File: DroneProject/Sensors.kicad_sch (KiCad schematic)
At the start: 21 parts, among them U61 LSM6DSOTR, U62 TMAG5273C1QDBVR, U63 INA181A1IDBVR, U64 M24C02-WMN6TP

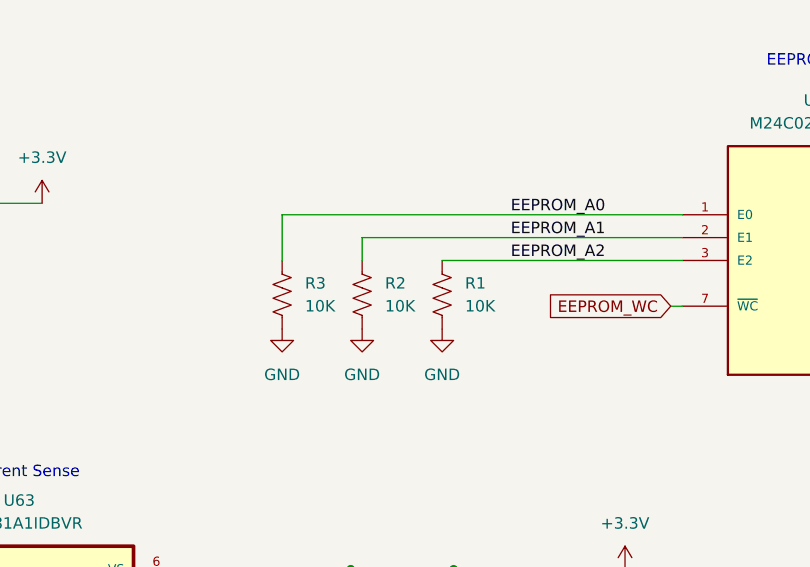
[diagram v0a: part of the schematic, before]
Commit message: Added test points
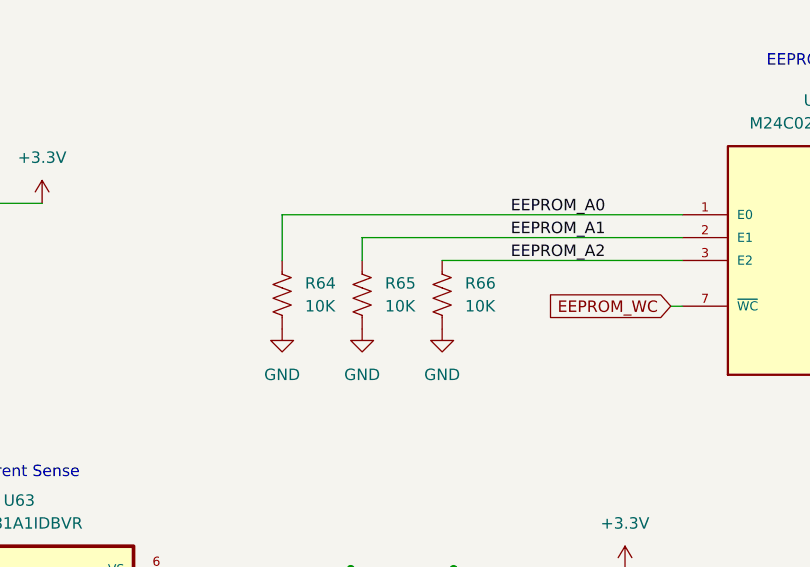
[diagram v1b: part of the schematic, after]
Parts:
- renumbered R3 to R64, R2 to R65, R1 to R66
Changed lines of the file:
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@@
 		(dnp no)
 		(fields_autoplaced yes)
-		(property "Reference" "R1"
+		(property "Reference" "R66"
 			(at 171.45 91.4399 0)
 			(effects
@@
 			(project "DroneProject"
 				(path "/feb4ca7b-5376-4689-a73b-f56020a5aa30/7cfdeeab-6878-42e6-abbb-2c878b968332"
-					(reference "R1")
+					(reference "R66")
 					(unit 1)
 				)
@@
 		(dnp no)
 		(fields_autoplaced yes)
-		(property "Reference" "R3"
+		(property "Reference" "R64"
 			(at 153.67 91.4399 0)
 			(effects
@@
 			(project "DroneProject"
 				(path "/feb4ca7b-5376-4689-a73b-f56020a5aa30/7cfdeeab-6878-42e6-abbb-2c878b968332"
-					(reference "R3")
+					(reference "R64")
 					(unit 1)
 				)
@@
 		(dnp no)
 		(fields_autoplaced yes)
-		(property "Reference" "R2"
+		(property "Reference" "R65"
 			(at 162.56 91.4399 0)
 			(effects
@@
 			(project "DroneProject"
 				(path "/feb4ca7b-5376-4689-a73b-f56020a5aa30/7cfdeeab-6878-42e6-abbb-2c878b968332"
-					(reference "R2")
-					(unit 1)
-				)
+					(reference "R65")
+					(unit 1)
+				)

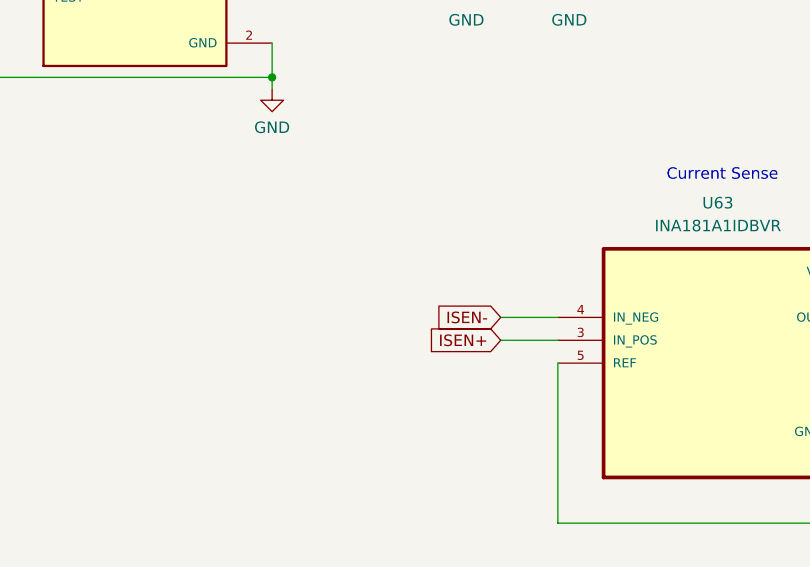
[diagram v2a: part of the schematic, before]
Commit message: Finished initial PCB layout.  However decided to go ahead and add the motor drivers for the first prototype anyways.  Re-did the reverse-polarity detection to use an NMOS instead of a PMOS.  Added sheets for each motor, still need to decide on parts.
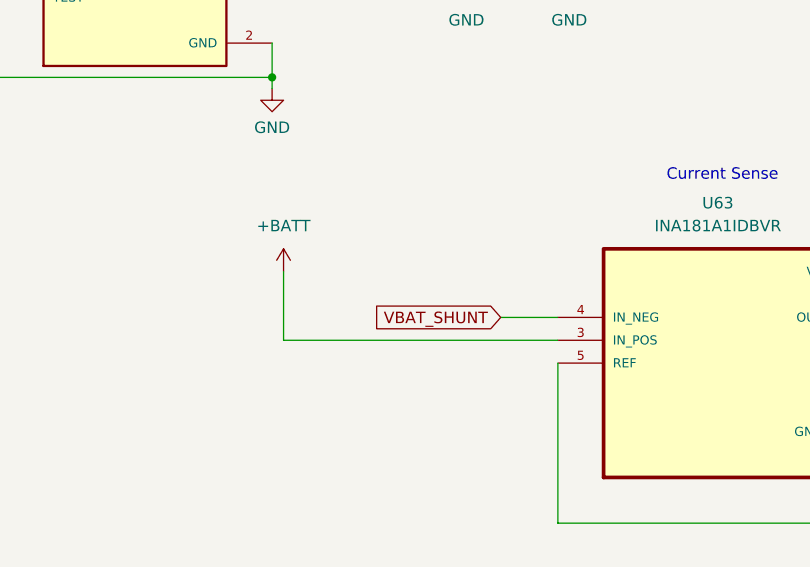
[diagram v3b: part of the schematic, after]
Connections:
- net ISEN+ renamed +BATT
- net ISEN- renamed VBAT_SHUNT
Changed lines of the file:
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@@
+	(wire
+		(pts
+			(xy 72.39 101.6) (xy 72.39 102.87)
+		)
+		(stroke
+			(width 0)
+			(type default)
+		)
+	)
+	(wire
+		(pts
+			(xy 93.98 82.55) (xy 105.41 82.55)
+		)
+		(stroke
+			(width 0)
+			(type default)
+		)
+	)
+	(wire
+		(pts
+			(xy 160.02 88.9) (xy 160.02 86.36)
+		)
+		(stroke
+			(width 0)
+			(type default)
+		)
+	)
+	(wire
+		(pts
+			(xy 92.71 36.83) (xy 95.25 36.83)
+		)
+		(stroke
+			(width 0)
+			(type default)
+		)
+	)
+	(wire
+		(pts
+			(xy 226.06 83.82) (xy 228.6 83.82)
+		)
+		(stroke
+			(width 0)
+			(type default)
+		)
+	)
+	(wire
+		(pts
+			(xy 151.13 88.9) (xy 151.13 83.82)
+		)
+		(stroke
+			(width 0)
+			(type default)
+		)
+	)
 	(wire
 		(pts
@@
 	(wire
 		(pts
-			(xy 72.39 101.6) (xy 72.39 102.87)
-		)
-		(stroke
-			(width 0)
-			(type default)
-		)
-	)
-	(wire
-		(pts
-			(xy 93.98 82.55) (xy 105.41 82.55)
-		)
-		(stroke
-			(width 0)
-			(type default)
-		)
-	)
-	(wire
-		(pts
-			(xy 160.02 88.9) (xy 160.02 86.36)
-		)
-		(stroke
-			(width 0)
-			(type default)
-		)
-	)
-	(wire
-		(pts
-			(xy 92.71 36.83) (xy 95.25 36.83)
-		)
-		(stroke
-			(width 0)
-			(type default)
-		)
-	)
-	(wire
-		(pts
-			(xy 226.06 83.82) (xy 228.6 83.82)
-		)
-		(stroke
-			(width 0)
-			(type default)
-		)
-	)
-	(wire
-		(pts
-			(xy 151.13 88.9) (xy 151.13 83.82)
-		)
-		(stroke
-			(width 0)
-			(type default)
-		)
-	)
-	(wire
-		(pts
 			(xy 55.88 46.99) (xy 67.31 46.99)
 		)
@@
 	(wire
 		(pts
+			(xy 73.66 123.19) (xy 73.66 130.81)
+		)
+		(stroke
+			(width 0)
+			(type default)
+		)
+	)
+	(wire
+		(pts
 			(xy 151.13 83.82) (xy 195.58 83.82)
 		)
@@
 	(wire
 		(pts
+			(xy 104.14 130.81) (xy 73.66 130.81)
+		)
+		(stroke
+			(width 0)
+			(type default)
+		)
+	)
+	(wire
+		(pts
 			(xy 226.06 78.74) (xy 247.65 78.74)
 		)
@@
 		(pts
 			(xy 83.82 39.37) (xy 95.25 39.37)
-		)
-		(stroke
-			(width 0)
-			(type default)
-		)
-	)
-	(wire
-		(pts
-			(xy 97.79 130.81) (xy 104.14 130.81)
 		)
 		(stroke
@@
 		)
 	)
-	(global_label "ISEN-"
+	(global_label "VBAT_SHUNT"
 		(shape input)
 		(at 97.79 128.27 180)
@@
 		)
 		(property "Intersheetrefs" "${INTERSHEET_REFS}"
-			(at 88.9386 128.27 0)
+			(at 83.2538 128.27 0)
 			(effects
 				(font
@@
 		)
 	)
-	(global_label "ISEN+"
+	(global_label "I2C1_SCL"
 		(shape input)
-		(at 97.79 130.81 180)
+		(at 74.93 87.63 0)
 		(fields_autoplaced yes)
 		(effects
@@
 				(size 1.27 1.27)
 			)
-			(justify right)
-		)
-		(property "Intersheetrefs" "${INTERSHEET_REFS}"
-			(at 88.9386 130.81 0)
-			(effects
-				(font
-					(size 1.27 1.27)
-				)
-				(justify right)
-			)
-		)
-	)
-	(global_label "I2C1_SCL"
-		(shape input)
-		(at 74.93 87.63 0)
-		(fields_autoplaced yes)
-		(effects
-			(font
-				(size 1.27 1.27)
-			)
 			(justify left)
 		)
@@
 					(unit 1)
 				)
+			)
+		)
+	)
+	(symbol
+		(lib_id "power:+BATT")
+		(at 73.66 123.19 0)
+		(unit 1)
+		(exclude_from_sim no)
+		(in_bom yes)
+		(on_board yes)
+		(dnp no)
+		(fields_autoplaced yes)
+		(property "Reference" "#PWR07"
+			(at 73.66 127 0)
+			(effects
+				(font
+					(size 1.27 1.27)
+				)
+				(hide yes)
+			)
+		)
+		(property "Value" "+BATT"
+			(at 73.66 118.11 0)
+			(effects
+				(font
+					(size 1.27 1.27)
+				)
+			)
+		)
+		(property "Footprint" ""
+			(at 73.66 123.19 0)
+			(effects
+				(font
+					(size 1.27 1.27)
+				)
+				(hide yes)
+			)
+		)
+		(property "Datasheet" ""
+			(at 73.66 123.19 0)
+			(effects
+				(font
+					(size 1.27 1.27)
+				)
+				(hide yes)
+			)
+		)
+		(property "Description" "Power symbol creates a global label with name \"+BATT\""
+			(at 73.66 123.19 0)
+			(effects
+				(font
+					(size 1.27 1.27)
+				)
+				(hide yes)
+			)
+		)
+		(pin "1"
+		)
+		(instances
+			(project ""
+				(path "/feb4ca7b-5376-4689-a73b-f56020a5aa30/7cfdeeab-6878-42e6-abbb-2c878b968332"
+					(reference "#PWR07")
+					(unit 1)
+				)

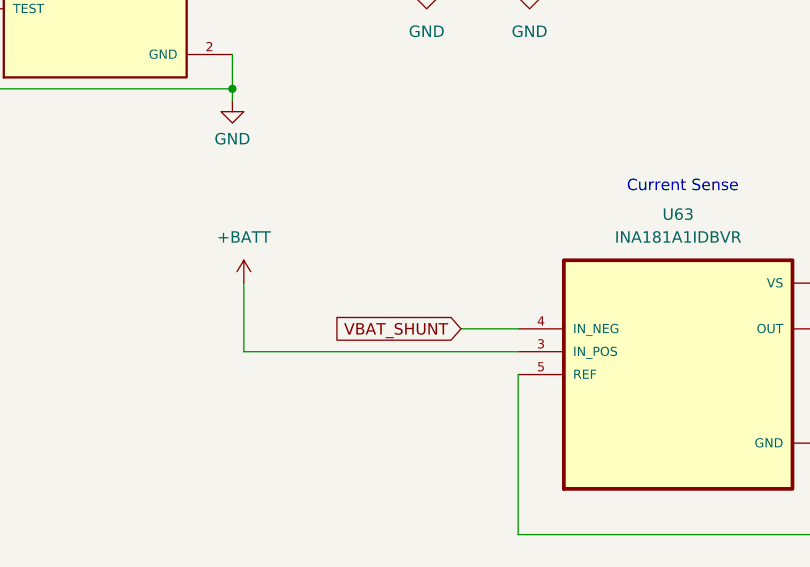
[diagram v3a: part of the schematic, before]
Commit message: Re-did layout for new power system
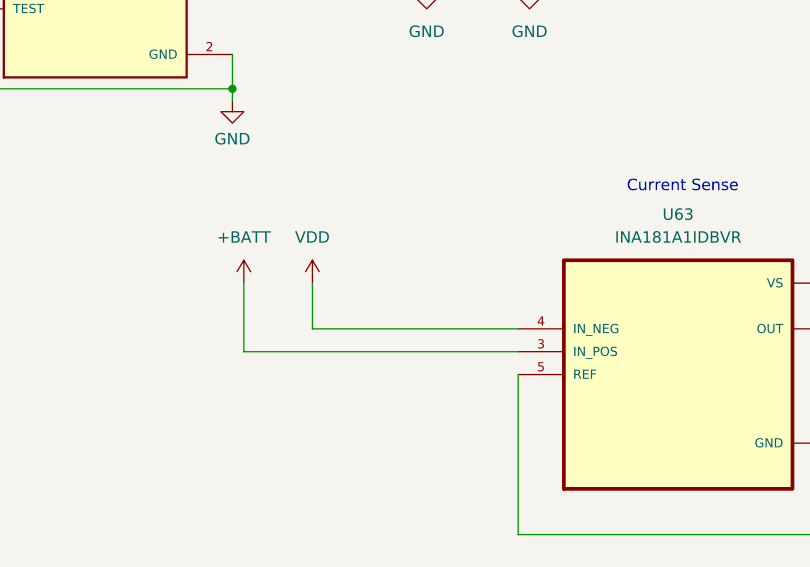
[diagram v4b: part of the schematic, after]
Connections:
- net VBAT_SHUNT renamed VDD
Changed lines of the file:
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@@
-	(wire
-		(pts
-			(xy 97.79 128.27) (xy 104.14 128.27)
-		)
-		(stroke
-			(width 0)
-			(type default)
-		)
-	)
 	(wire
 		(pts
@@
 	(wire
 		(pts
+			(xy 81.28 123.19) (xy 81.28 128.27)
+		)
+		(stroke
+			(width 0)
+			(type default)
+		)
+	)
+	(wire
+		(pts
 			(xy 24.13 46.99) (xy 24.13 43.18)
+		)
+		(stroke
+			(width 0)
+			(type default)
+		)
+	)
+	(wire
+		(pts
+			(xy 81.28 128.27) (xy 104.14 128.27)
 		)
 		(stroke
@@
 				)
 				(justify left)
-			)
-		)
-	)
-	(global_label "VBAT_SHUNT"
-		(shape input)
-		(at 97.79 128.27 180)
-		(fields_autoplaced yes)
-		(effects
-			(font
-				(size 1.27 1.27)
-			)
-			(justify right)
-		)
-		(property "Intersheetrefs" "${INTERSHEET_REFS}"
-			(at 83.2538 128.27 0)
-			(effects
-				(font
-					(size 1.27 1.27)
-				)
-				(justify right)
 			)
 		)
@@
 					(unit 1)
 				)
+			)
+		)
+	)
+	(symbol
+		(lib_id "power:VDD")
+		(at 81.28 123.19 0)
+		(unit 1)
+		(exclude_from_sim no)
+		(in_bom yes)
+		(on_board yes)
+		(dnp no)
+		(fields_autoplaced yes)
+		(property "Reference" "#PWR097"
+			(at 81.28 127 0)
+			(effects
+				(font
+					(size 1.27 1.27)
+				)
+				(hide yes)
+			)
+		)
+		(property "Value" "VDD"
+			(at 81.28 118.11 0)
+			(effects
+				(font
+					(size 1.27 1.27)
+				)
+			)
+		)
+		(property "Footprint" ""
+			(at 81.28 123.19 0)
+			(effects
+				(font
+					(size 1.27 1.27)
+				)
+				(hide yes)
+			)
+		)
+		(property "Datasheet" ""
+			(at 81.28 123.19 0)
+			(effects
+				(font
+					(size 1.27 1.27)
+				)
+				(hide yes)
+			)
+		)
+		(property "Description" "Power symbol creates a global label with name \"VDD\""
+			(at 81.28 123.19 0)
+			(effects
+				(font
+					(size 1.27 1.27)
+				)
+				(hide yes)
+			)
+		)
+		(pin "1"
+		)
+		(instances
+			(project ""
+				(path "/feb4ca7b-5376-4689-a73b-f56020a5aa30/7cfdeeab-6878-42e6-abbb-2c878b968332"
+					(reference "#PWR097")
+					(unit 1)
+				)

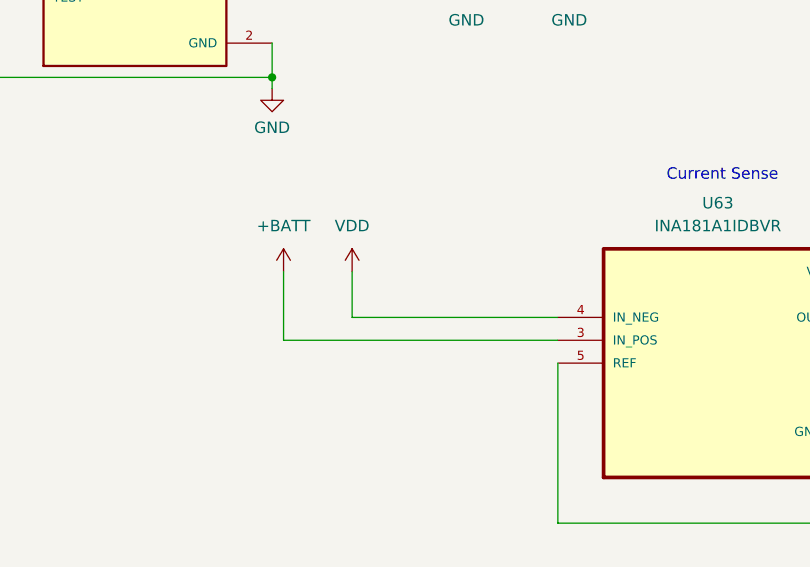
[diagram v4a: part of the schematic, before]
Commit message: Added a second MCU for motor control.  Removed 5V rail.  Added COM switching for SWD and UART external headers
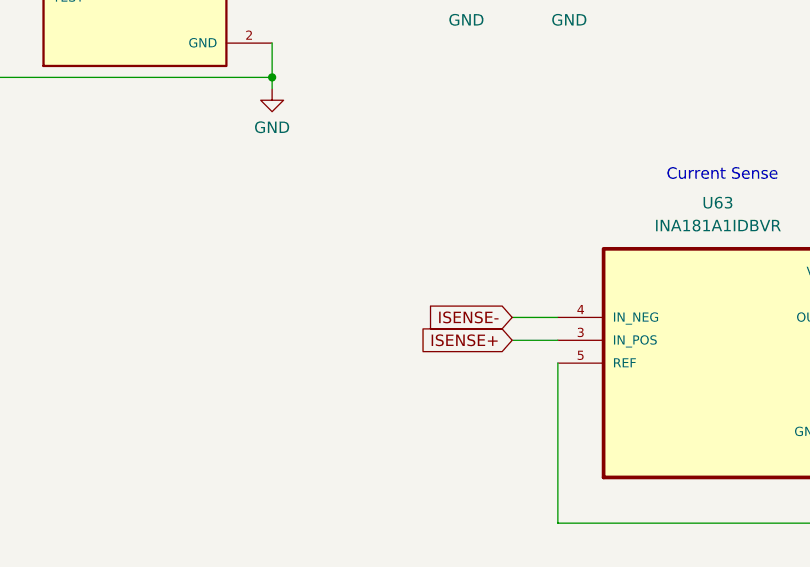
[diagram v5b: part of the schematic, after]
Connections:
- net +BATT renamed ISENSE+
- net VDD renamed ISENSE-
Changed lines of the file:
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@@
-	(wire
-		(pts
-			(xy 73.66 123.19) (xy 73.66 130.81)
-		)
-		(stroke
-			(width 0)
-			(type default)
-		)
-	)
 	(wire
 		(pts
@@
 	(wire
 		(pts
-			(xy 81.28 123.19) (xy 81.28 128.27)
-		)
-		(stroke
-			(width 0)
-			(type default)
-		)
-	)
-	(wire
-		(pts
 			(xy 24.13 46.99) (xy 24.13 43.18)
 		)
@@
 	(wire
 		(pts
-			(xy 81.28 128.27) (xy 104.14 128.27)
-		)
-		(stroke
-			(width 0)
-			(type default)
-		)
-	)
-	(wire
-		(pts
 			(xy 26.67 46.99) (xy 24.13 46.99)
 		)
@@
 	(wire
 		(pts
-			(xy 104.14 130.81) (xy 73.66 130.81)
-		)
-		(stroke
-			(width 0)
-			(type default)
-		)
-	)
-	(wire
-		(pts
 			(xy 226.06 78.74) (xy 247.65 78.74)
 		)
@@
 	(wire
 		(pts
+			(xy 99.06 128.27) (xy 104.14 128.27)
+		)
+		(stroke
+			(width 0)
+			(type default)
+		)
+	)
+	(wire
+		(pts
 			(xy 139.7 128.27) (xy 142.24 128.27)
 		)
@@
 		(pts
 			(xy 67.31 46.99) (xy 83.82 46.99)
+		)
+		(stroke
+			(width 0)
+			(type default)
+		)
+	)
+	(wire
+		(pts
+			(xy 99.06 130.81) (xy 104.14 130.81)
 		)
 		(stroke
@@
 		)
 	)
+	(global_label "ISENSE+"
+		(shape input)
+		(at 99.06 130.81 180)
+		(fields_autoplaced yes)
+		(effects
+			(font
+				(size 1.27 1.27)
+			)
+			(justify right)
+		)
+		(property "Intersheetrefs" "${INTERSHEET_REFS}"
+			(at 87.8501 130.81 0)
+			(effects
+				(font
+					(size 1.27 1.27)
+				)
+				(justify right)
+			)
+		)
+	)
 	(global_label "I2C1_SDA"
 		(shape bidirectional)
@@
 		)
 	)
+	(global_label "ISENSE-"
+		(shape input)
+		(at 99.06 128.27 180)
+		(fields_autoplaced yes)
+		(effects
+			(font
+				(size 1.27 1.27)
+			)
+			(justify right)
+		)
+		(property "Intersheetrefs" "${INTERSHEET_REFS}"
+			(at 87.8501 128.27 0)
+			(effects
+				(font
+					(size 1.27 1.27)
+				)
+				(justify right)
+			)
+		)
+	)
 	(global_label "I2C1_SCL"
 		(shape input)
@@
 	)
 	(symbol
-		(lib_id "power:VDD")
-		(at 81.28 123.19 0)
-		(unit 1)
-		(exclude_from_sim no)
-		(in_bom yes)
-		(on_board yes)
-		(dnp no)
-		(fields_autoplaced yes)
-		(property "Reference" "#PWR097"
-			(at 81.28 127 0)
-			(effects
-				(font
-					(size 1.27 1.27)
-				)
-				(hide yes)
-			)
-		)
-		(property "Value" "VDD"
-			(at 81.28 118.11 0)
-			(effects
-				(font
-					(size 1.27 1.27)
-				)
-			)
-		)
-		(property "Footprint" ""
-			(at 81.28 123.19 0)
-			(effects
-				(font
-					(size 1.27 1.27)
-				)
-				(hide yes)
-			)
-		)
-		(property "Datasheet" ""
-			(at 81.28 123.19 0)
-			(effects
-				(font
-					(size 1.27 1.27)
-				)
-				(hide yes)
-			)
-		)
-		(property "Description" "Power symbol creates a global label with name \"VDD\""
-			(at 81.28 123.19 0)
-			(effects
-				(font
-					(size 1.27 1.27)
-				)
-				(hide yes)
-			)
-		)
-		(pin "1"
-		)
-		(instances
-			(project ""
-				(path "/feb4ca7b-5376-4689-a73b-f56020a5aa30/7cfdeeab-6878-42e6-abbb-2c878b968332"
-					(reference "#PWR097")
-					(unit 1)
-				)
-			)
-		)
-	)
-	(symbol
 		(lib_id "power:+3.3V")
 		(at 190.5 44.45 0)
@@
 					(unit 1)
 				)
-			)
-		)
-	)
-	(symbol
-		(lib_id "power:+BATT")
-		(at 73.66 123.19 0)
-		(unit 1)
-		(exclude_from_sim no)
-		(in_bom yes)
-		(on_board yes)
-		(dnp no)
-		(fields_autoplaced yes)
-		(property "Reference" "#PWR07"
-			(at 73.66 127 0)
-			(effects
-				(font
-					(size 1.27 1.27)
-				)
-				(hide yes)
-			)
-		)
-		(property "Value" "+BATT"
-			(at 73.66 118.11 0)
-			(effects
-				(font
-					(size 1.27 1.27)
-				)
-			)
-		)
-		(property "Footprint" ""
-			(at 73.66 123.19 0)
-			(effects
-				(font
-					(size 1.27 1.27)
-				)
-				(hide yes)
-			)
-		)
-		(property "Datasheet" ""
-			(at 73.66 123.19 0)
-			(effects
-				(font
-					(size 1.27 1.27)
-				)
-				(hide yes)
-			)
-		)
-		(property "Description" "Power symbol creates a global label with name \"+BATT\""
-			(at 73.66 123.19 0)
-			(effects
-				(font
-					(size 1.27 1.27)
-				)
-				(hide yes)
-			)
-		)
-		(pin "1"
-		)
-		(instances
-			(project ""
-				(path "/feb4ca7b-5376-4689-a73b-f56020a5aa30/7cfdeeab-6878-42e6-abbb-2c878b968332"
-					(reference "#PWR07")
-					(unit 1)
-				)
